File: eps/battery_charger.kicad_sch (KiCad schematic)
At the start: 8 parts

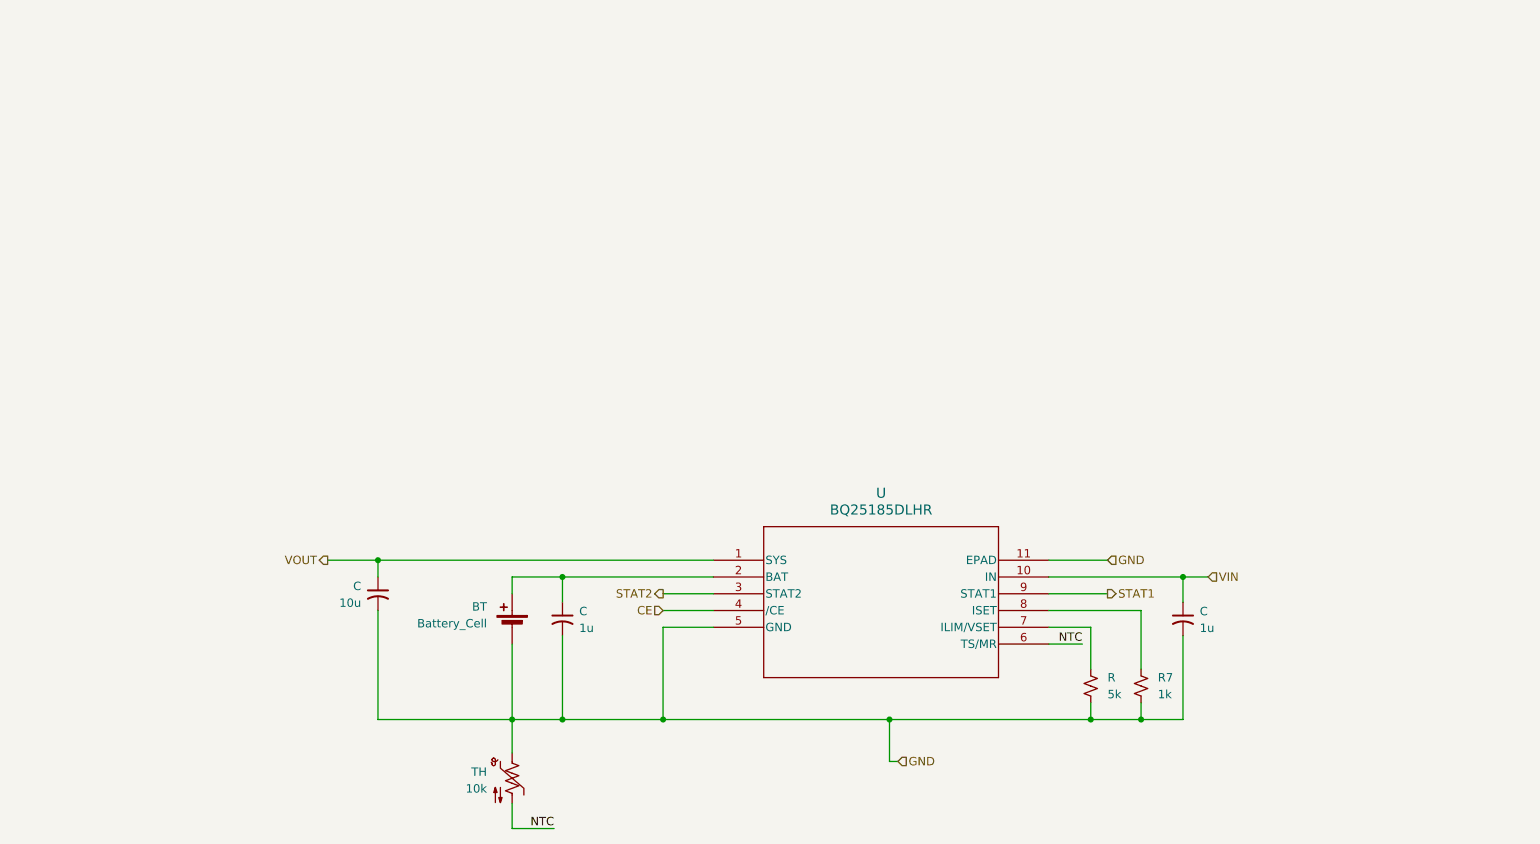
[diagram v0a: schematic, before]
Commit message: start migration to custom battery charger symbol
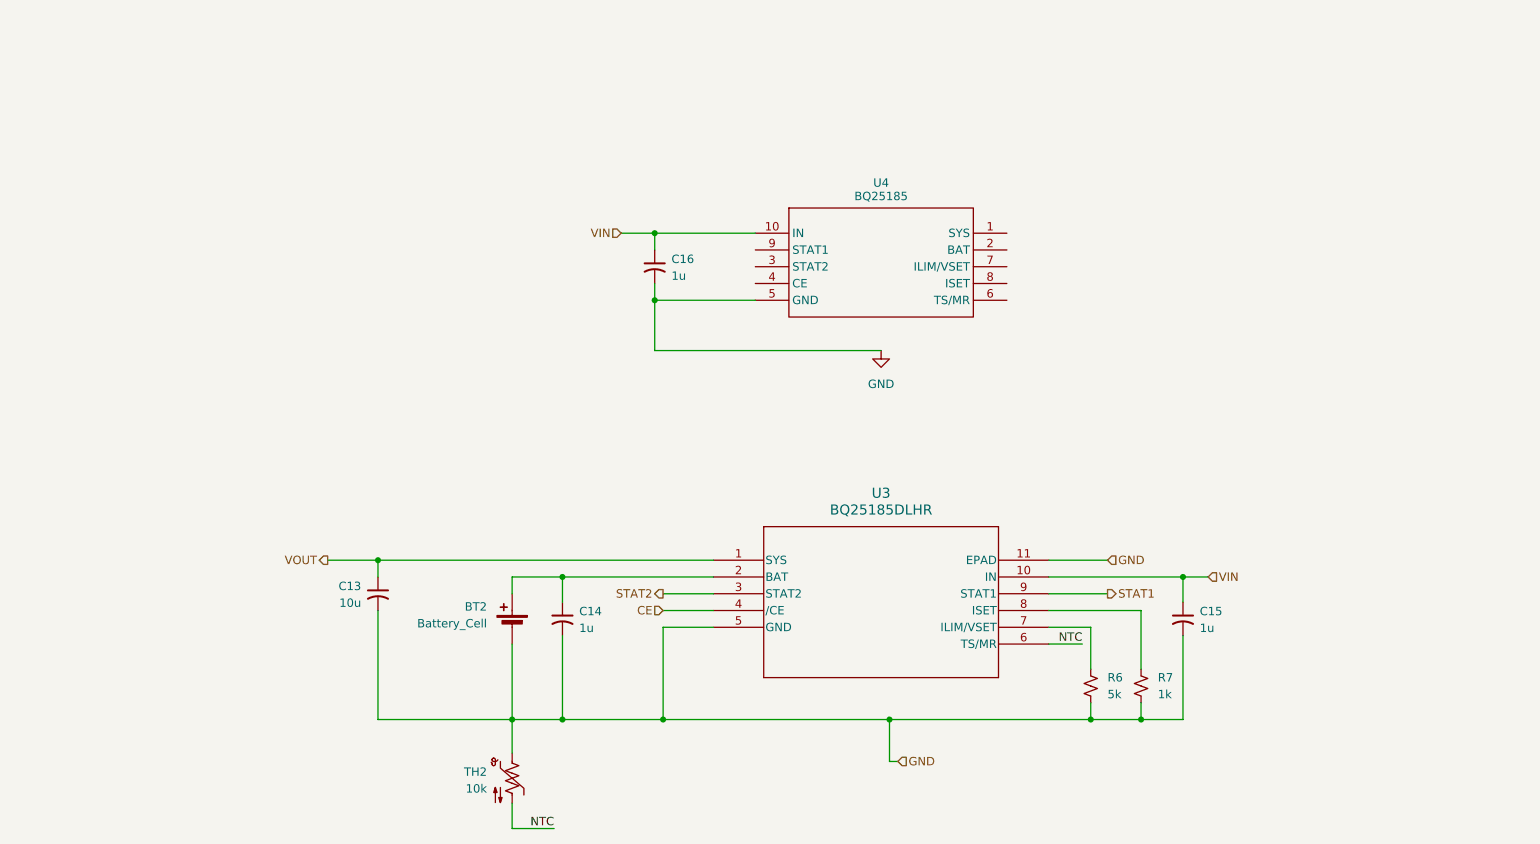
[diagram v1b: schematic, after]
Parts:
- added C16: 1u, symbol Device:C_Small_US
- added U4: BQ25185, symbol BQ25185DLHR:BQ25185
- renumbered BT to BT2, C to C13, C to C14, C to C15, R to R6, TH to TH2, U to U3
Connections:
- net GND: now also C16.2, U4.5 (GND)
- net VIN: now also C16.1, U4.10 (IN)

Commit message: finish implementing custom BQ25185 symbol
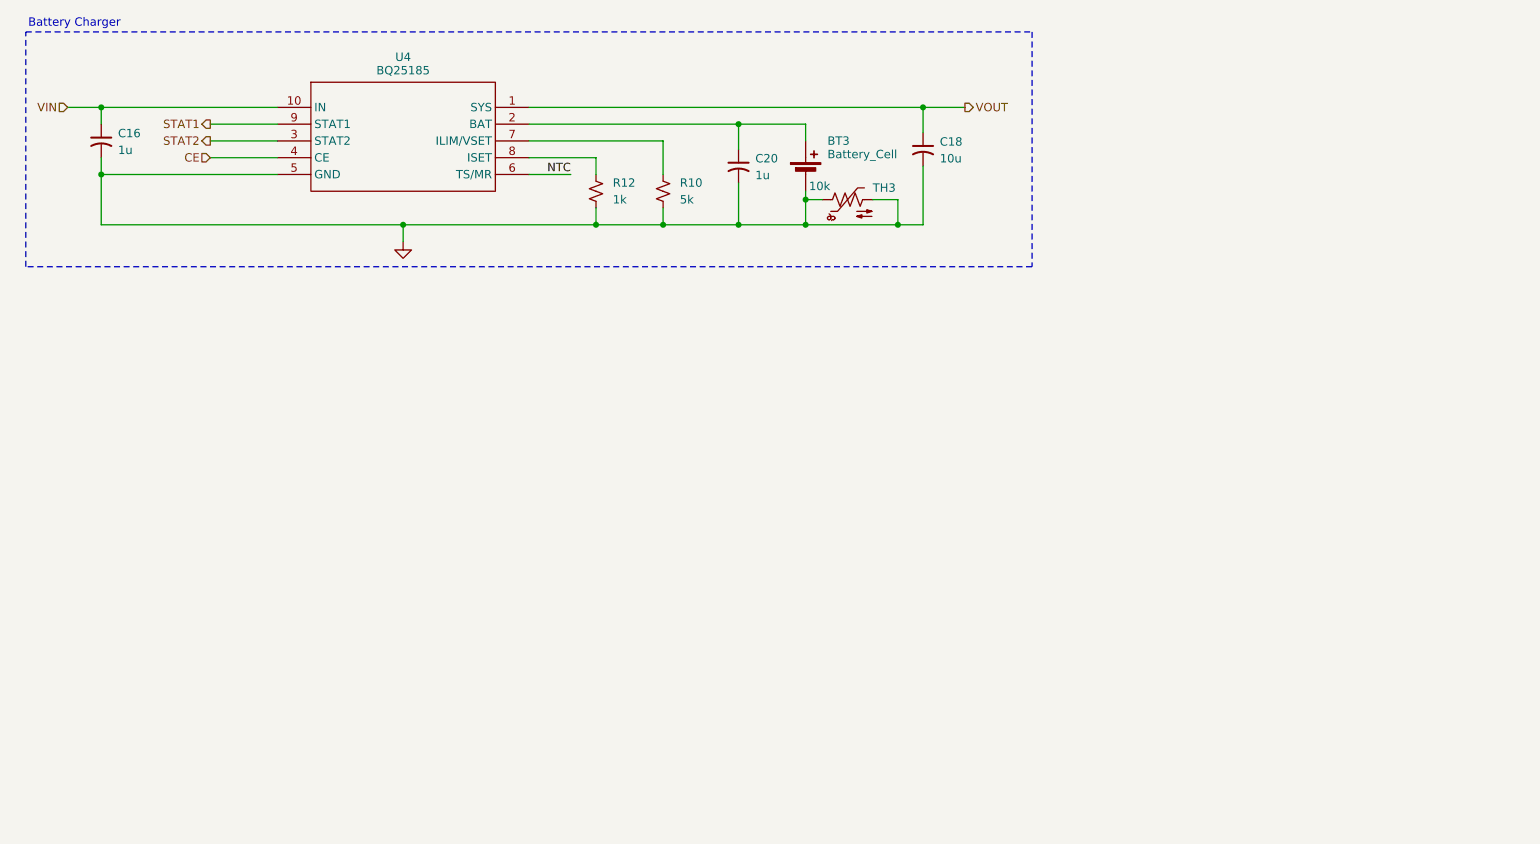
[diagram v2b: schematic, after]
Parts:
- removed BT2: Battery_Cell, symbol Device:Battery_Cell
- removed C13: 10u, symbol Device:C_Small_US
- removed C14, C15: 1u, symbol Device:C_Small_US
- removed R6: 5k, symbol Device:R_Small_US
- removed R7: 1k, symbol Device:R_Small_US
- removed TH2: 10k, symbol Device:Thermistor_NTC_US
- removed U3: BQ25185DLHR, footprints:WSON10_DLH_TEX, symbol BQ25185DLHR:BQ25185DLHR
- added BT3: Battery_Cell, symbol Device:Battery_Cell
- added C18: 10u, symbol Device:C_Small_US
- added C20: 1u, symbol Device:C_Small_US
- added R10: 5k, symbol Device:R_Small_US
- added R12: 1k, symbol Device:R_Small_US
- added TH3: 10k, symbol Device:Thermistor_NTC_US
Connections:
- net CE: now also U4.4 (CE)
- net GND: now also BT3.2 (-), C18.2, C20.2, R10.2, R12.2, TH3.1, TH3.2
- net NTC: now also U4.6 (TS/MR)
- net STAT1: now also U4.9 (STAT1)
- net STAT2: now also U4.3 (STAT2)
- net VOUT: now also U4.1 (SYS), C18.1
- net at U4.2 (BAT): now also BT3.1 (+), C20.1
- net at U4.7 (ILIM/VSET): now also R10.1
- net at U4.8 (ISET): now also R12.1
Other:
- note added: "Battery Charger"
- moved on the sheet: C16, U4

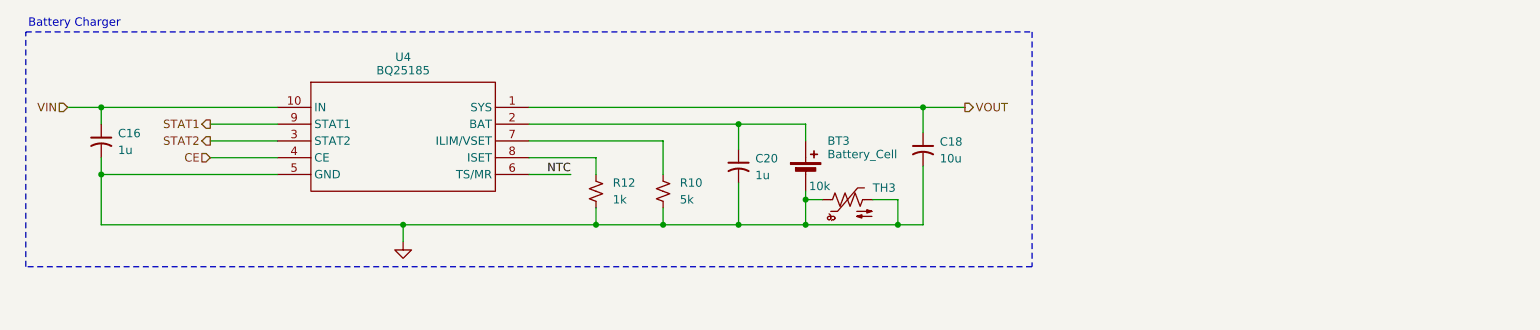
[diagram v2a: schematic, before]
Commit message: add ideal diode controller to battery charger
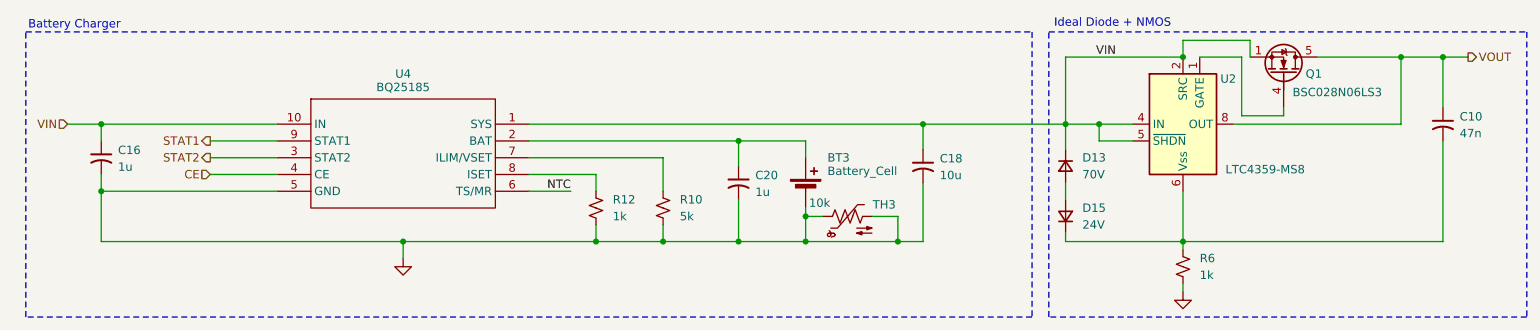
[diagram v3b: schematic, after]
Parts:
- added C10: 47n, symbol Device:C_Small_US
- added D13: 70V, symbol Device:D_Small
- added D15: 24V, symbol Device:D_Small
- added Q1: BSC028N06LS3, Package_TO_SOT_SMD:TDSON-8-1, symbol Transistor_FET:BSC028N06LS3
- added R6: 1k, symbol Device:R_Small_US
- added U2: LTC4359-MS8, Package_SO:MSOP-8_3x3mm_P0.65mm, symbol Power_Management:LTC4359-MS8
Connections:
- net GND: now also R6.2
- net VIN: now also C18.1, U4.1 (SYS), D13.1 (K), Q1.1 (S), Q1.2 (S), Q1.3 (S), U2.2 (SRC), U2.4 (IN), U2.5 (~{SHDN})
- net VOUT: now also C10.1, Q1.5 (D), U2.8 (OUT); no longer C18.1, U4.1 (SYS)
- new net: D13.2 (A), D15.2 (A)
- new net: C10.2, D15.1 (K), R6.1, U2.6 (Vss)
- new net: Q1.4 (G), U2.1 (GATE)
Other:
- note added: "Ideal Diode + NMOS"
- moved on the sheet: BT3, C16, C18, C20, R10, R12, TH3, U4
